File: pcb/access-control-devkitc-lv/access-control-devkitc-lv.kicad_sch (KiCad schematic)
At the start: 41 parts, among them J1 CON_I2C, K1 G5LE-1, U1 ESP32-DevKitC

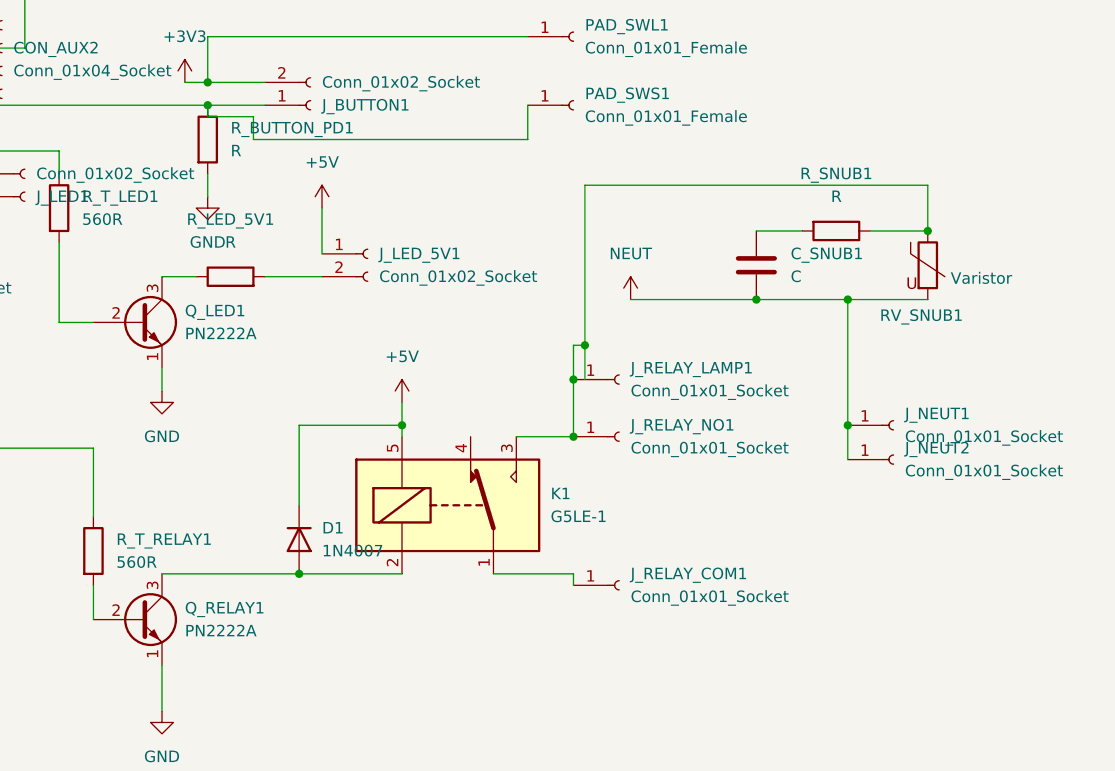
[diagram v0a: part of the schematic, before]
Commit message: Split board into Low Voltage / Relay modules
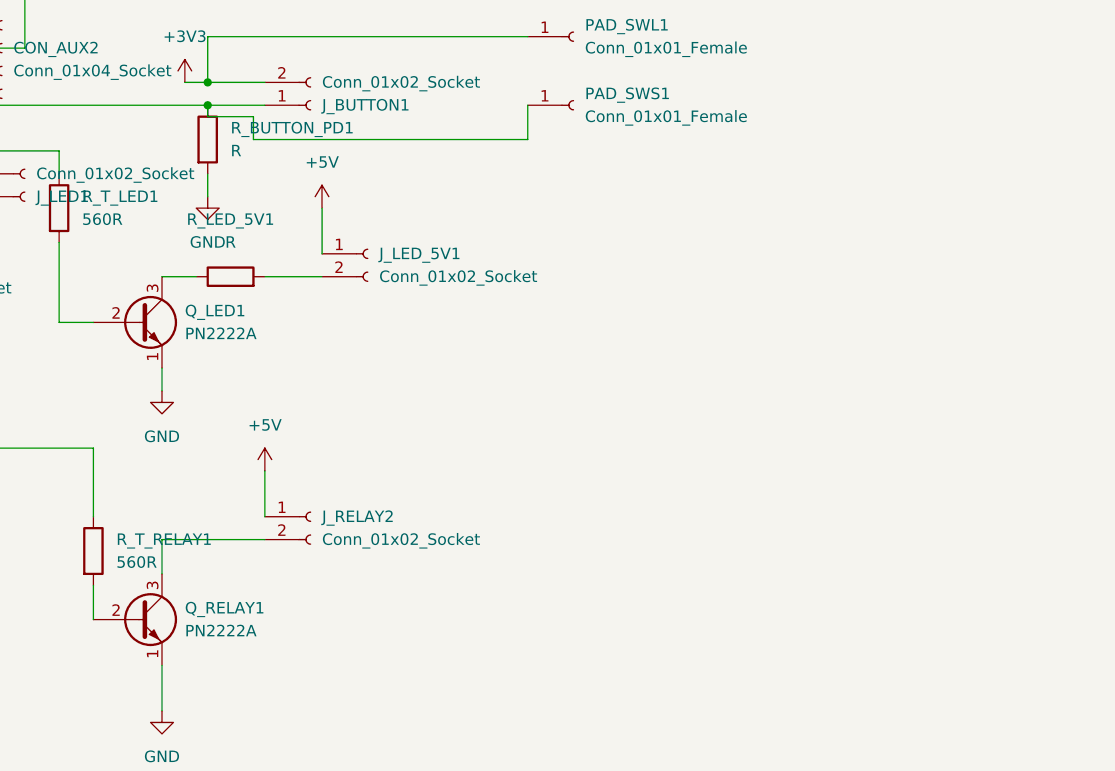
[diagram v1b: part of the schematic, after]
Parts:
- removed C_SNUB1: C, Capacitor_THT:CP_Axial_L10.0mm_D6.0mm_P15.00mm_Horizontal, symbol Device:C
- removed D1: 1N4007, Diode_THT:D_DO-41_SOD81_P10.16mm_Horizontal, symbol Diode:1N4007
- removed J_NEUT1, J_NEUT2, J_RELAY_COM1, J_RELAY_LAMP1, J_RELAY_NO1: Conn_01x01_Socket, Connector_Wire:SolderWire-2.5sqmm_1x01_D2.4mm_OD4.4mm, symbol Connector:Conn_01x01_Socket
- removed K1: G5LE-1, Relay_THT:Relay_SPDT_Omron-G5LE-1, symbol Relay:G5LE-1
- removed RV_SNUB1: Varistor, Varistor:RV_Disc_D12mm_W3.9mm_P7.5mm, symbol Device:Varistor
- removed R_SNUB1: R, Resistor_THT:R_Axial_DIN0617_L17.0mm_D6.0mm_P20.32mm_Horizontal, symbol Device:R
- added J_RELAY2: Conn_01x02_Socket, Connector_PinHeader_2.54mm:PinHeader_1x02_P2.54mm_Vertical, symbol Connector:Conn_01x02_Socket
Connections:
- net +5V: now also J_RELAY2.1 (Pin_1)
- net at Q_RELAY1.3 (C): now also J_RELAY2.2 (Pin_2)

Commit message: Update with values
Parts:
- removed J_5V1, J_GND1: Conn_01x01_Socket, Connector_Wire:SolderWire-2.5sqmm_1x01_D2.4mm_OD4.4mm, symbol Connector:Conn_01x01_Socket
- added J_5V1: Conn_01x02_Socket, Connector_PinHeader_2.54mm:PinHeader_1x02_P2.54mm_Vertical, symbol Connector:Conn_01x02_Socket
- C_5V_De1: footprint Capacitor_THT:C_Axial_L5.1mm_D3.1mm_P10.00mm_Horizontal -> Capacitor_THT:C_Disc_D4.3mm_W1.9mm_P5.00mm
- C_5V_Med1: footprint Capacitor_THT:C_Axial_L5.1mm_D3.1mm_P10.00mm_Horizontal -> Capacitor_THT:C_Disc_D5.0mm_W2.5mm_P5.00mm
- J_RELAY2: footprint Connector_PinHeader_2.54mm:PinHeader_1x02_P2.54mm_Vertical -> Connector_PinHeader_2.54mm:PinHeader_1x04_P2.54mm_Vertical; symbol Connector:Conn_01x02_Socket -> Connector:Conn_01x04_Pin
- R_BOOT_SERIAL1, R_BUTTON_PD1: value R -> 10kR
- R_LED_5V1: value R -> 330R
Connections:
- net +5V: now also J_5V1.1 (Pin_1)
- net GND: now also J_RELAY2.4 (Pin_4), J_5V1.2 (Pin_2)
- net at Q_RELAY1.2 (B), R_T_RELAY1.2: now also J_RELAY2.3 (Pin_3)

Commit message: Updates for manufacturing
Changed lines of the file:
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@@
+	)
+	(junction
+		(at 251.46 60.96)
+		(diameter 0)
+		(color 0 0 0 0)
 	)
 	(junction
@@
 	)
 	(junction
+		(at 251.46 52.07)
+		(diameter 0)
+		(color 0 0 0 0)
+	)
+	(junction
 		(at 166.37 63.5)
 		(diameter 0)
@@
 	(wire
 		(pts
-			(xy 251.46 63.5) (xy 251.46 59.69)
+			(xy 251.46 63.5) (xy 251.46 60.96)
 		)
 		(stroke
@@
 	(wire
 		(pts
+			(xy 251.46 53.34) (xy 251.46 52.07)
+		)
+		(stroke
+			(width 0)
+			(type default)
+		)
+	)
+	(wire
+		(pts
 			(xy 187.96 50.8) (xy 172.72 50.8)
 		)
@@
 	(wire
 		(pts
+			(xy 279.4 53.34) (xy 251.46 53.34)
+		)
+		(stroke
+			(width 0)
+			(type default)
+		)
+	)
+	(wire
+		(pts
 			(xy 154.94 35.56) (xy 149.86 35.56)
 		)
@@
 	(wire
 		(pts
+			(xy 251.46 60.96) (xy 251.46 59.69)
+		)
+		(stroke
+			(width 0)
+			(type default)
+		)
+	)
+	(wire
+		(pts
 			(xy 176.53 49.53) (xy 157.48 49.53)
 		)
@@
 		)
 		(stroke
+			(width 0)
+			(type default)
+		)
+	)
+	(wire
+		(pts
+			(xy 251.46 60.96) (xy 279.4 60.96)
+		)
+		(stroke

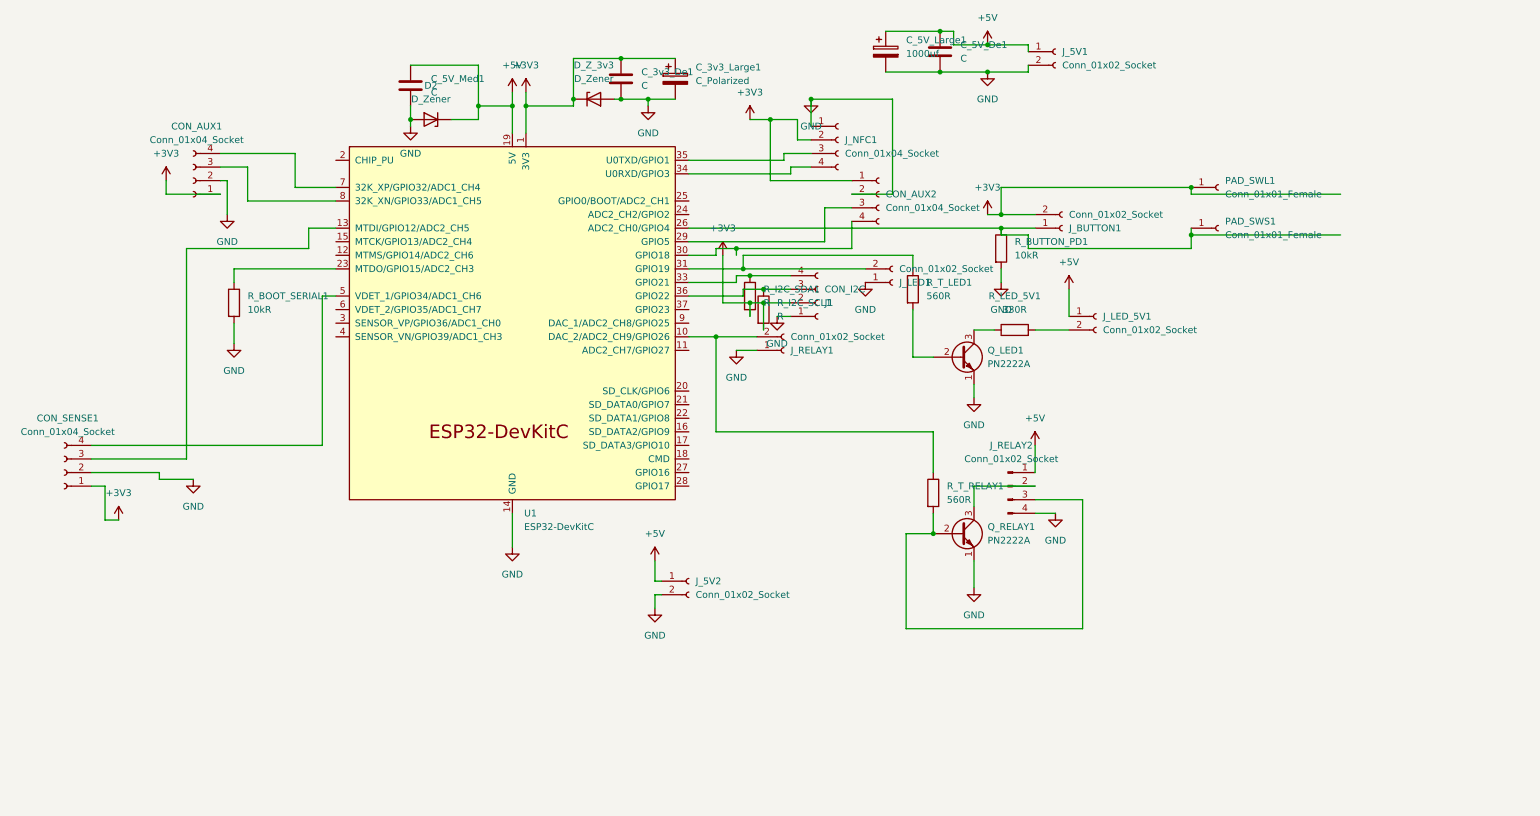
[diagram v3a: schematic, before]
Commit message: Redability updates to schematic
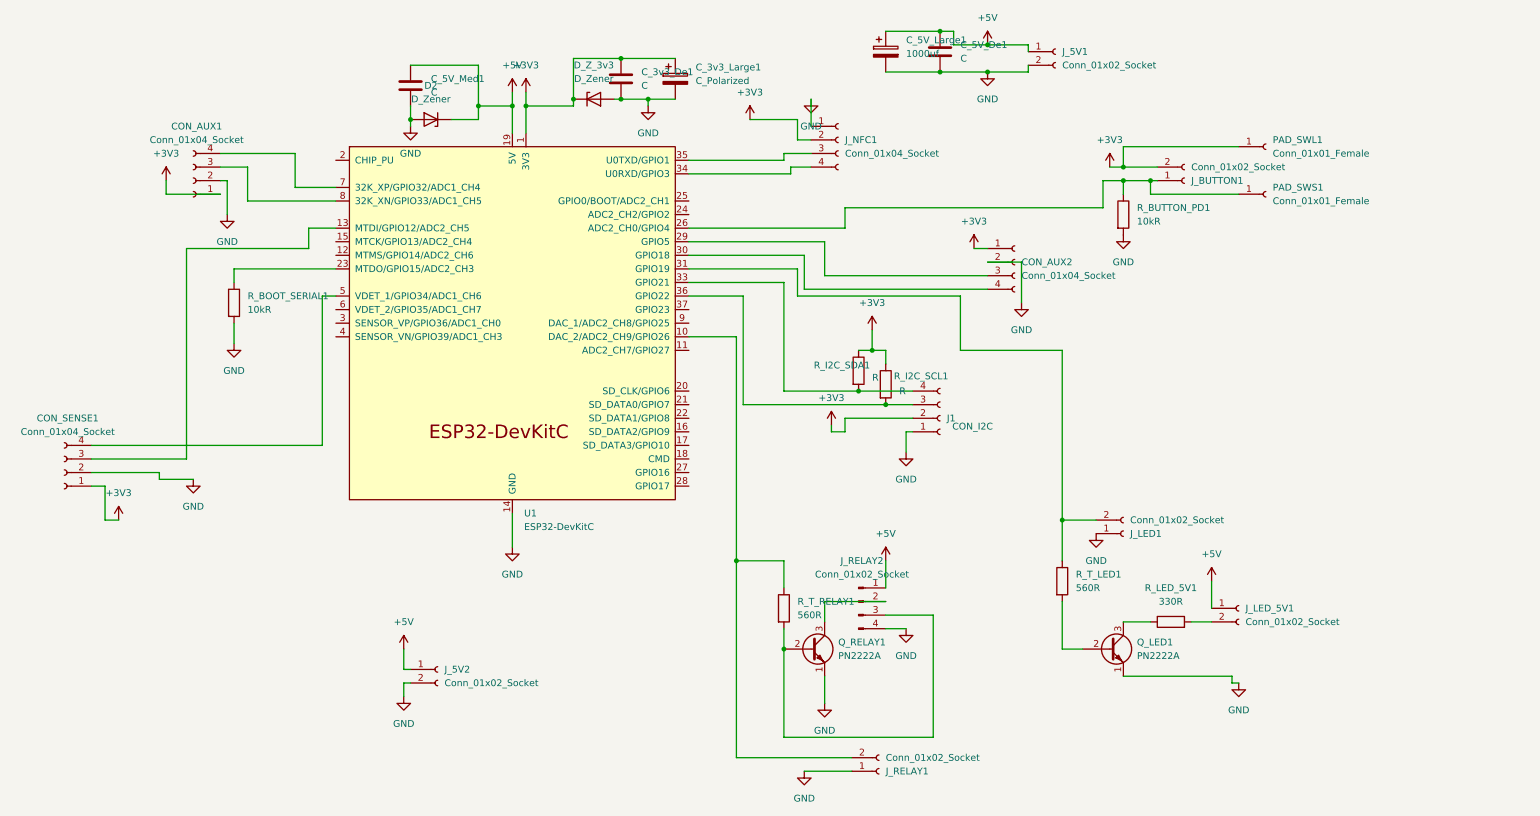
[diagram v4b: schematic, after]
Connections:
- net +3V3: now also R_I2C_SCL1.1, R_I2C_SDA1.1; no longer R_I2C_SCL1.2, R_I2C_SDA1.2
- net at J1.3 (Pin_3), U1.36 (GPIO22): now also R_I2C_SCL1.2; no longer R_I2C_SCL1.1
- net at J1.4 (Pin_4), U1.33 (GPIO21): now also R_I2C_SDA1.2; no longer R_I2C_SDA1.1
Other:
- moved on the sheet: CON_AUX2, J1, J_5V2, J_BUTTON1, J_LED1, J_LED_5V1, J_RELAY1, J_RELAY2, PAD_SWL1, PAD_SWS1, Q_LED1, Q_RELAY1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
